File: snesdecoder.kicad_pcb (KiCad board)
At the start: 2 copper layers, 36.2 x 20.2 mm, 17 parts, among them J1 SNES Controller Input, J2 UpDownLeftRight, J3 AB, J4 XY, J5 StartSel, J6 LR, J7 Power, U1 74HC04, U2 74LS161, U3 TPIC6C596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

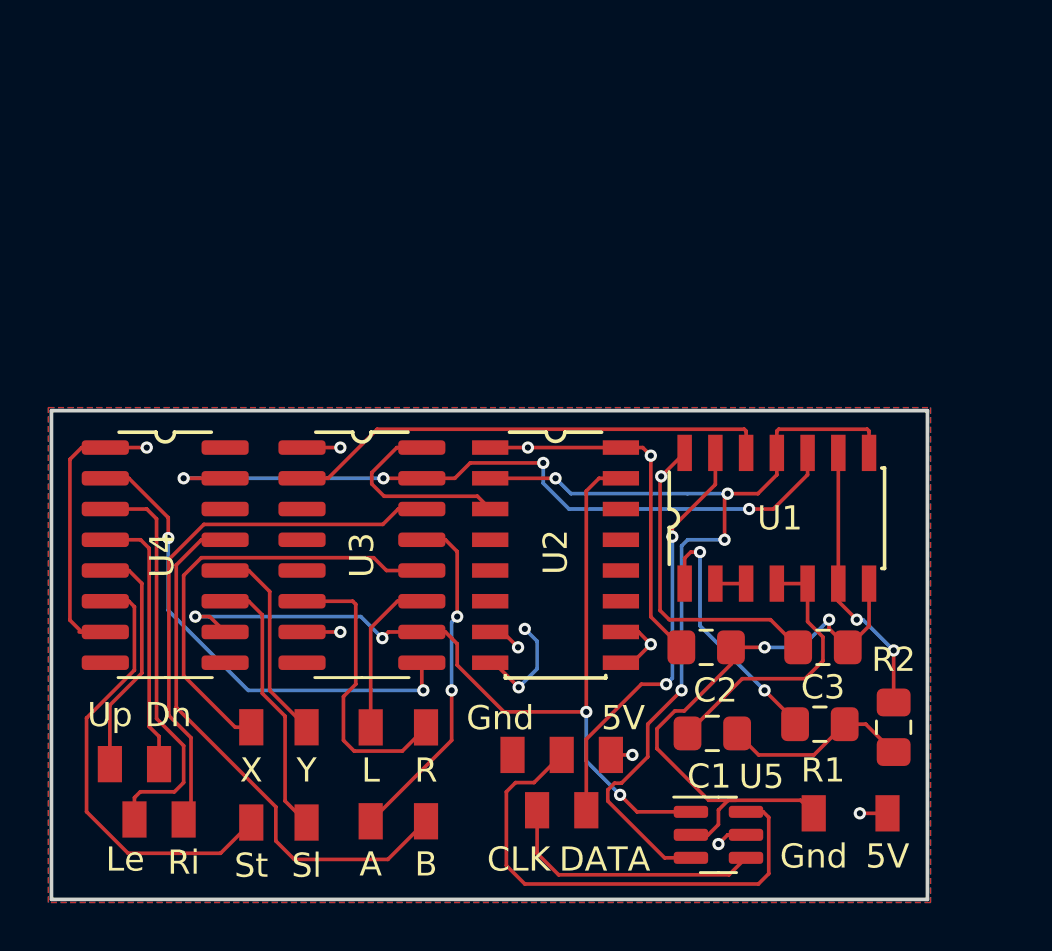
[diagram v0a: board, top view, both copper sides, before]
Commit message: update to V2: change schema, pcb layout, datasheets
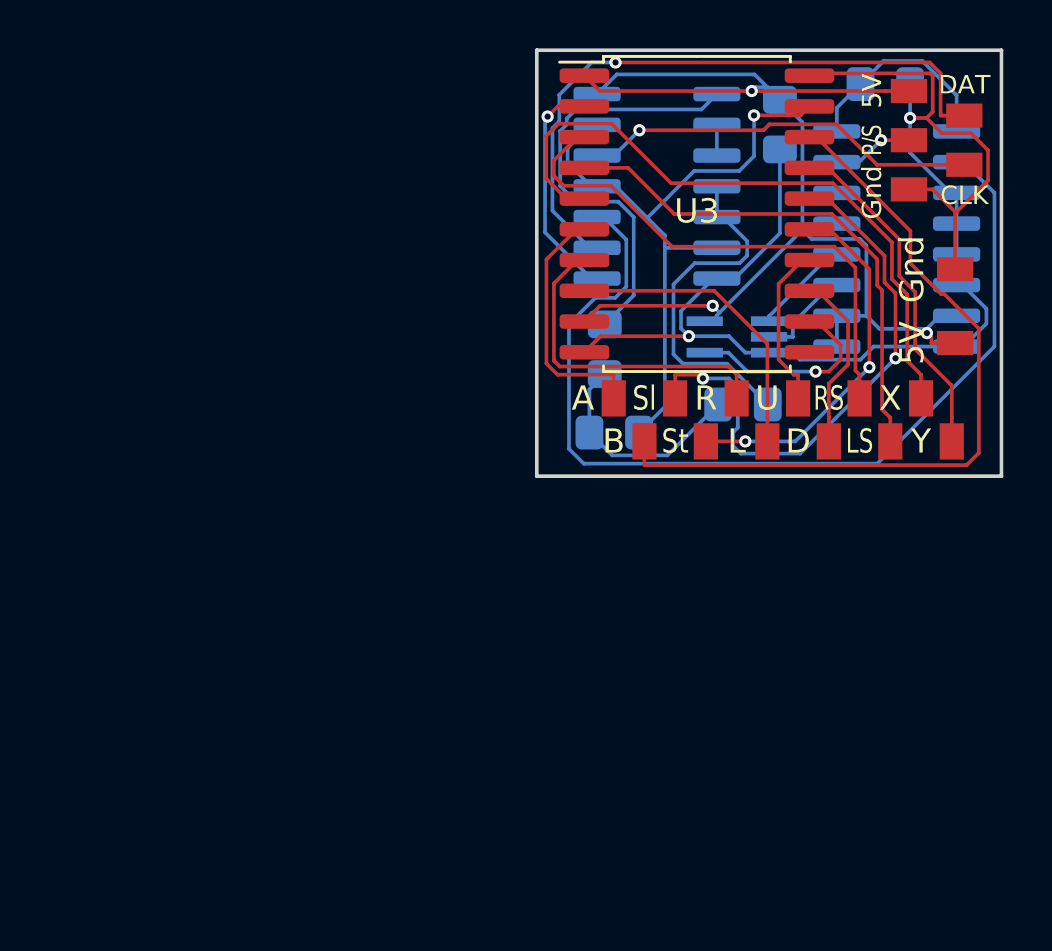
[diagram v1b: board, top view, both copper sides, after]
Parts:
- removed J4: XY, IO:2PAD_XY
- removed J5: StartSel, IO:2PAD_StartSel
- removed J6: LR, IO:2PAD_LR
- removed J7: Power, IO:2PAD_Pwrr
- removed U5: 74LVC2G17, Package_SO:SC-74-6_1.5x2.9mm_P0.95mm
- C1, C2, C3, R1, R2, U1, U2: moved to B.Cu
- J2: value UpDownLeftRight -> Power; footprint IO:4PAD_DIR -> IO:2PAD_Pwrr
- J3: value AB -> 12PAD; footprint IO:2PAD_AB -> IO:12PAD
- U3: value TPIC6C596 -> TLC6C5912; footprint Package_SO:SOIC-16_3.9x9.9mm_P1.27mm -> Package_SO:SOIC-20W_7.5x12.8mm_P1.27mm
- U4: value TPIC6C596 -> 74LVC1G08; footprint Package_SO:SOIC-16_3.9x9.9mm_P1.27mm -> Package_TO_SOT_SMD:SOT-353_SC-70-5_Handsoldering; moved to B.Cu
- moved J2 39.0 mm to (173.1, 87.4), turned to 270 degrees
- moved J1 27.1 mm to (168.7, 80.5), turned to 90 degrees
- moved U4 25.3 mm to (163.1, 88.6), turned to 180 degrees
- moved C2 24.4 mm to (169.2, 78.2)
- moved J3 21.9 mm to (164.2, 91.8)
- moved C3 21.7 mm to (164.8, 79.9), turned to 90 degrees
- moved U3 19.8 mm to (161.4, 83.6)
- moved U2 19.2 mm to (169.7, 84.6), turned to 180 degrees
- moved R1 17.9 mm to (157.6, 89.2), turned to 270 degrees
- moved R2 16.8 mm to (158.0, 92.6), turned to 180 degrees
- moved U1 14.6 mm to (159.8, 82.4), turned to 180 degrees
- moved C1 13.6 mm to (163.3, 91.4), turned to 180 degrees
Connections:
- J2 pad 1: Net-(J2-Pad1) -> GND
- J2 pad 2: Net-(J2-Pad2) -> +5V
- R1 pad 1: Net-(C1-Pad2) -> Net-(R1-Pad1)
- R1 pad 2: Net-(R1-Pad2) -> Net-(C1-Pad2)
- R2 pad 1: Net-(C1-Pad2) -> Net-(R2-Pad1)
- R2 pad 2: Net-(R2-Pad2) -> Net-(C1-Pad2)
- U1 pad 1: Net-(R1-Pad2) -> Net-(R1-Pad1)
- U1 pad 11: Net-(U1-Pad11) -> Net-(R2-Pad1)
- U1 pad 12: Net-(U1-Pad12) -> Net-(J1-Pad2)
- U1 pad 13: Net-(J1-Pad4) -> Net-(R2-Pad1)
- U1 pad 6: Net-(R2-Pad2) -> Net-(R2-Pad1)
- U1 pad 8: Net-(U1-Pad11) -> Net-(U1-Pad8)
- U1 pad 9: Net-(R2-Pad2) -> Net-(J1-Pad4)
- U2 pad 15: Net-(U2-Pad15) -> Net-(J1-Pad3)
- U2 pad 2: Net-(U1-Pad11) -> Net-(U1-Pad10)
- U3 pad 10: Net-(U2-Pad15) -> GND
- U3 pad 12: Net-(J4-Pad1) -> Net-(U3-Pad12)
- U3 pad 13: Net-(J3-Pad1) -> Net-(J3-Pad8)
- U3 pad 14: Net-(J2-Pad4) -> Net-(J3-Pad7)
- U3 pad 15: Net-(U1-Pad10) -> Net-(J3-Pad4)
- U3 pad 16: GND -> Net-(J3-Pad3)
- U3 pad 2: Net-(U1-Pad12) -> Net-(U1-Pad8)
- U3 pad 3: Net-(U3-Pad3) -> Net-(J3-Pad9)
- U3 pad 4: Net-(U3-Pad4) -> Net-(J3-Pad10)
- U3 pad 5: Net-(U3-Pad5) -> Net-(J3-Pad11)
- U3 pad 6: Net-(J6-Pad2) -> Net-(J3-Pad1)
- U3 pad 7: +5V -> Net-(J3-Pad5)
- U3 pad 8: GND -> Net-(J3-Pad6)
- U3 pad 9: Net-(U3-Pad9) -> +5V
- U4 pad 1: +5V -> Net-(U2-Pad12)
- U4 pad 2: Net-(U3-Pad9) -> Net-(U2-Pad11)
- U4 pad 3: Net-(J2-Pad3) -> GND
- U4 pad 4: Net-(J2-Pad2) -> Net-(U3-Pad12)
- U4 pad 5: Net-(J2-Pad1) -> +5V
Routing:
- net Net-(U1-Pad11): track 39.4 -> 0.00 mm, vias 4 -> 0
- net Net-(U2-Pad15): track 38.0 -> 0.00 mm, vias 4 -> 0
- net Net-(R2-Pad1): track 0.00 -> 27.8 mm, vias 0 -> 1
- net Net-(J3-Pad11): track 0.00 -> 27.1 mm
- net Net-(J3-Pad3): track 0.00 -> 23.3 mm, vias 0 -> 2
- net Net-(J2-Pad4): track 22.6 -> 0.00 mm
- net Net-(J3-Pad9): track 0.00 -> 21.8 mm
- net Net-(J3-Pad10): track 0.00 -> 21.4 mm
- net Net-(U3-Pad9): track 20.2 -> 0.00 mm, vias 2 -> 0
- net Net-(U1-Pad12): track 20.1 -> 0.00 mm
- net GND: track 38.1 -> 58.1 mm, vias 4 -> 2
- net Net-(J4-Pad1): track 18.7 -> 0.00 mm
- net Net-(J5-Pad1): track 18.6 -> 0.00 mm
- net Net-(R1-Pad1): track 0.00 -> 18.0 mm
- net Net-(J1-Pad3): track 20.7 -> 3.36 mm, vias 0 -> 1
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- removed copper zone on B.Cu, net +5V
- removed copper zone on F.Cu, net GND
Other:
- board size 36.2 x 20.2 mm -> 19.2 x 17.6 mm

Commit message: snesdecoder compact release
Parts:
- U1: footprint Package_SO:SOIC-14_3.9x8.7mm_P1.27mm -> Package_SO:TSSOP-14_4.4x5mm_P0.65mm
- U2: footprint Package_SO:SOIC-16_3.9x9.9mm_P1.27mm -> Package_SO:TSSOP-16_4.4x5mm_P0.65mm
- U3: footprint Package_SO:SOIC-20W_7.5x12.8mm_P1.27mm -> Package_SO:TSSOP-20_4.4x6.5mm_P0.65mm
- moved U2 15.9 mm to (154.1, 81.6), turned to 90 degrees
- moved R2 15.8 mm to (166.6, 79.4), turned to 90 degrees
- moved J3 14.1 mm to (159.0, 78.8)
- moved J2 13.6 mm to (159.5, 86.8), turned to 90 degrees
- moved C1 13.0 mm to (163.6, 78.4), turned to 0 degrees
- moved C2 10.8 mm to (161.0, 85.2), turned to 270 degrees
- moved R1 10.7 mm to (163.7, 80.3), turned to 0 degrees
- moved C3 7.00 mm to (157.9, 79.4)
- moved J1 7.00 mm to (163.5, 85.2)
- moved U3 6.88 mm to (154.8, 85.2), turned to 90 degrees
- moved U4 6.47 mm to (158.5, 84.1), turned to 270 degrees
- moved U1 5.69 mm to (164.7, 85.2), turned to 270 degrees
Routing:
- net Net-(J3-Pad2): track 31.2 -> 2.86 mm
- net Net-(U1-Pad10): track 40.0 -> 14.2 mm, vias 0 -> 2
- net Net-(J1-Pad4): track 26.6 -> 4.21 mm
- net +5V: track 64.5 -> 45.4 mm, vias 3 -> 5
- net Net-(J3-Pad3): track 23.3 -> 4.63 mm, vias 2 -> 0
- net Net-(R1-Pad1): track 18.0 -> 2.46 mm
- net Net-(J3-Pad12): track 14.2 -> 27.4 mm, vias 0 -> 2
- net Net-(J1-Pad2): track 16.4 -> 3.92 mm
- net Net-(J3-Pad4): track 15.2 -> 3.11 mm, vias 2 -> 0
- net Net-(J3-Pad11): track 27.1 -> 16.9 mm
- net GND: track 58.1 -> 67.9 mm, vias 2 -> 4
- net Net-(J1-Pad3): track 3.36 -> 12.8 mm
- net Net-(C1-Pad1): track 14.7 -> 5.51 mm
- net Net-(U1-Pad8): track 9.46 -> 17.1 mm
- net Net-(J3-Pad10): track 21.4 -> 14.3 mm
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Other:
- board size 19.2 x 17.6 mm -> 17.5 x 12.5 mm
